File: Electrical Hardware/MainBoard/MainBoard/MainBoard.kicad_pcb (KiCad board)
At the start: 2 copper layers, 49.4 x 51.7 mm, 76 parts, among them J1 SM02B-SRSS-TB_LFSN_, J2 Conn_01x04_Socket, J3 Conn_01x04_Socket, J4 Conn_01x04_Socket, J5 USB_B_Micro, J6 Thermistor, J7 62684-401100ALF, J8 Conn_01x02_Socket, SW1 SW_Push, SW2 SW_Push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

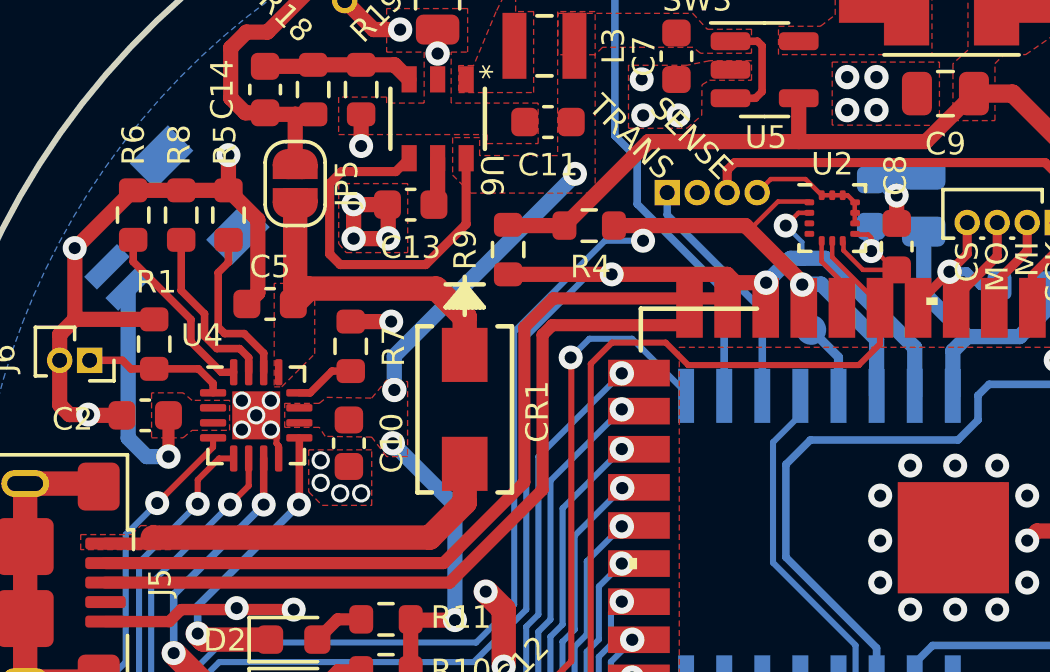
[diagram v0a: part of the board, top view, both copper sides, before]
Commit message: Expand LIS2D and BQ24074 footprint pads
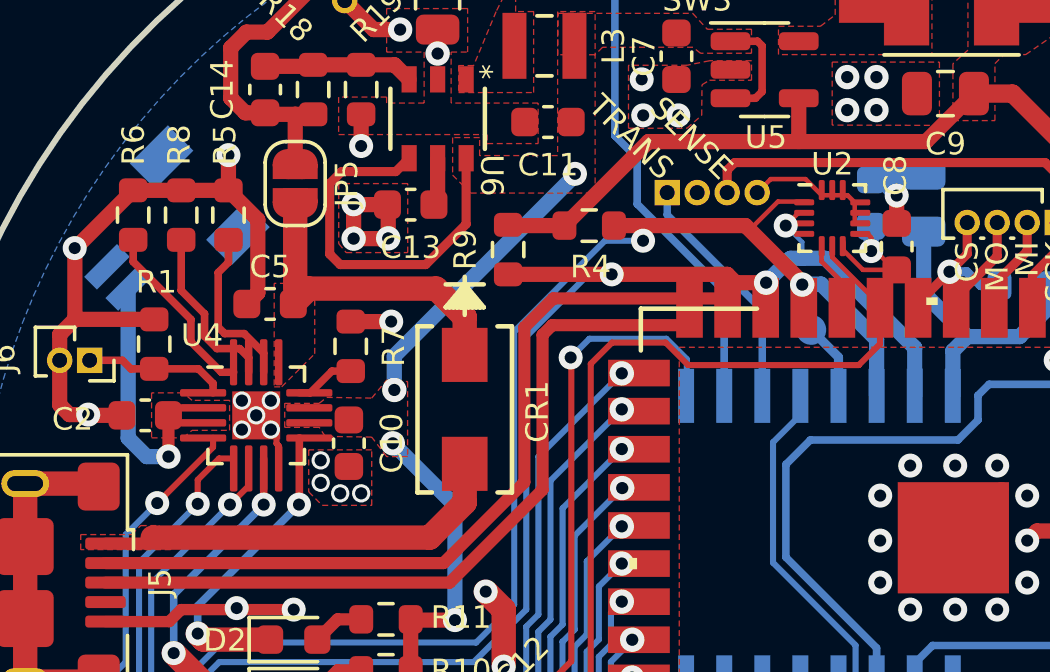
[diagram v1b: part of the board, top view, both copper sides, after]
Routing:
- net /BACKLIGHT: track 22.3 -> 23.0 mm

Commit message: LIS2d Layout
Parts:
- moved C8 1.71 mm to (101.2, 38.2)
- moved U2 0.84 mm to (99.1, 38.8)
- moved R3 0.27 mm to (108.7, 39.0)
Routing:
- net /CS: track 5.95 -> 2.59 mm, vias 1 -> 0
- net GND: track 150.5 -> 152.4 mm
- net /SENSE_P: track 17.8 -> 18.6 mm
- net Net-(JP1-B): track 13.2 -> 13.7 mm
- net +3.3V: track 138.5 -> 138.2 mm, vias 7 -> 6

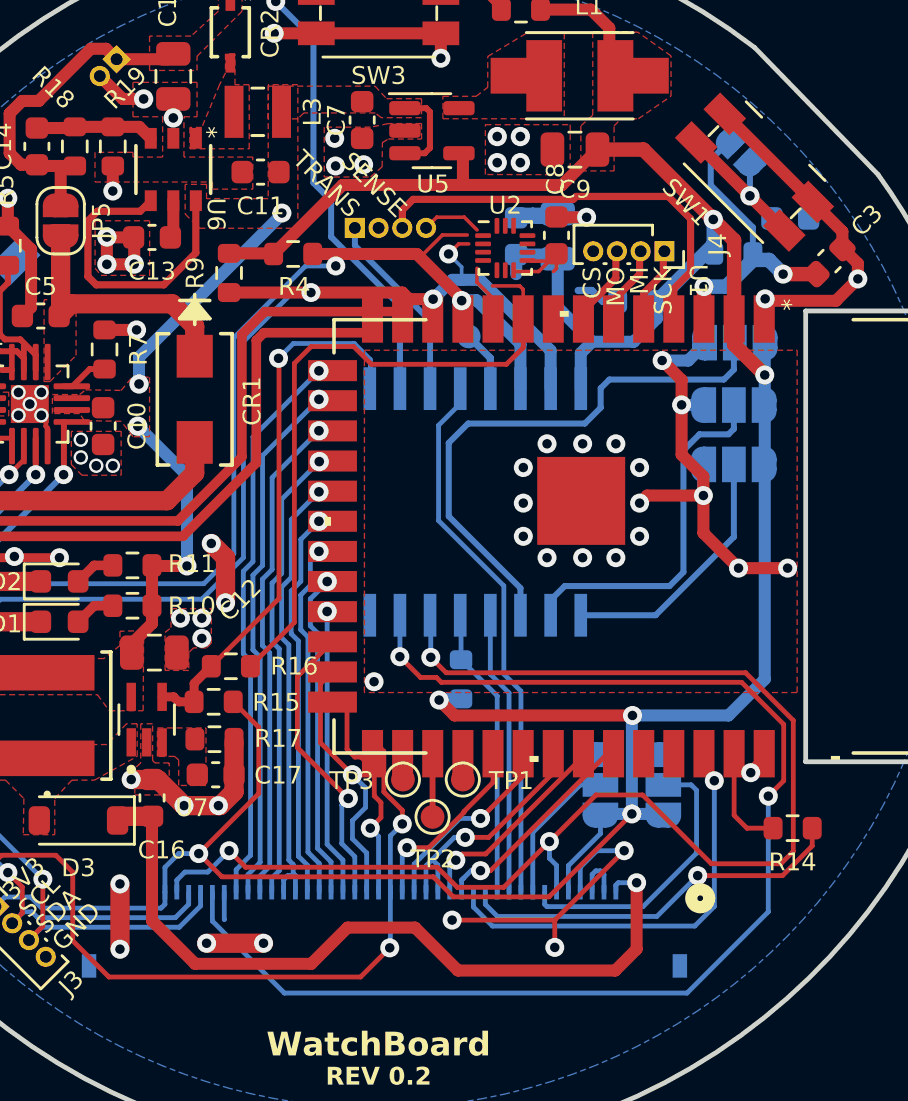
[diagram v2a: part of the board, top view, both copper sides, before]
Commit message: Wire LEDK and adjust wiring
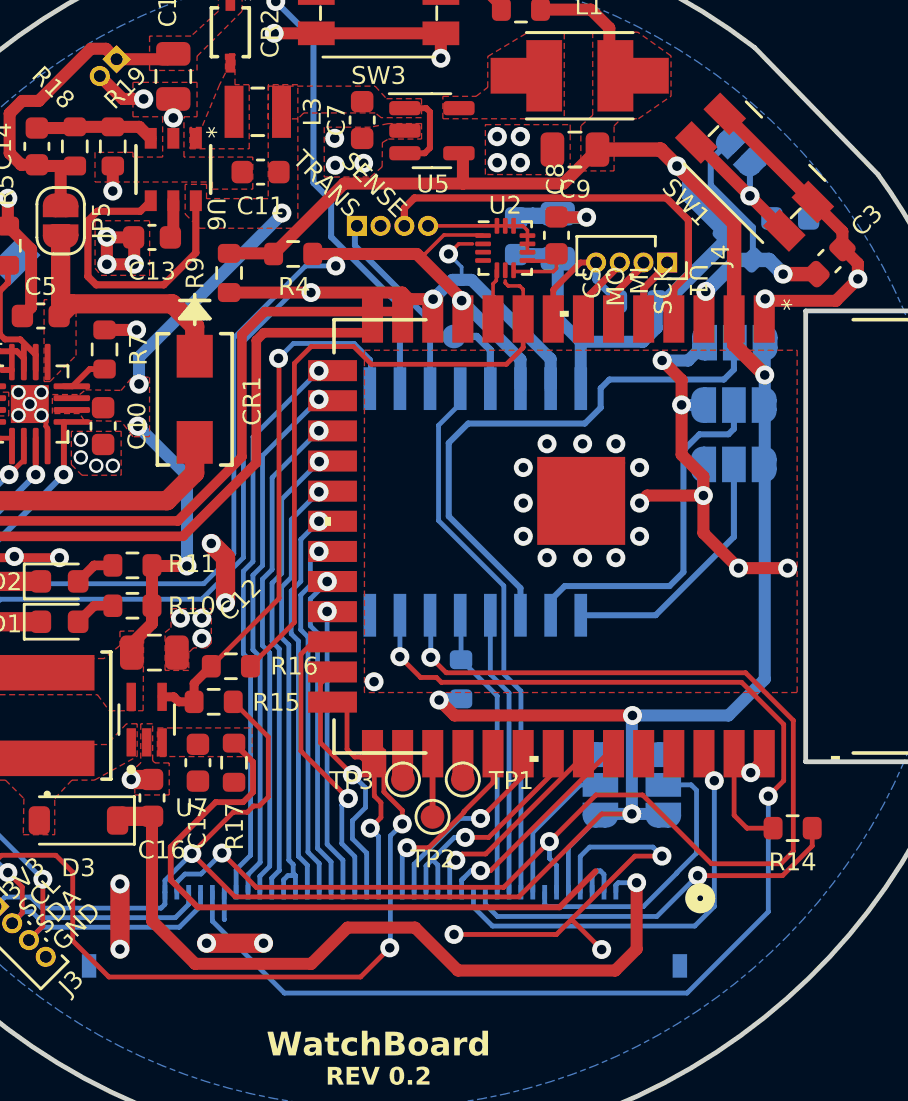
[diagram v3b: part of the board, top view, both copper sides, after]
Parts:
- moved R17 1.29 mm to (87.6, 60.5), turned to -90 degrees
- moved C17 0.91 mm to (86.1, 60.5), turned to -90 degrees
- moved TP4 0.62 mm to (96.9, 42.5)
- moved J4 0.49 mm to (105.9, 39.4)
- moved R3 0.39 mm to (108.9, 38.7), turned to -45 degrees
- moved J2 0.12 mm to (92.8, 37.8)
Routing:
- net /LEDK: track 2.12 -> 29.3 mm
- net +3.3V: track 138.2 -> 144.4 mm
- net /CS: track 2.59 -> 6.26 mm
- net /EXP_IRQ: track 2.58 -> 3.40 mm
- net GND: track 152.4 -> 153.2 mm, vias 68 -> 66

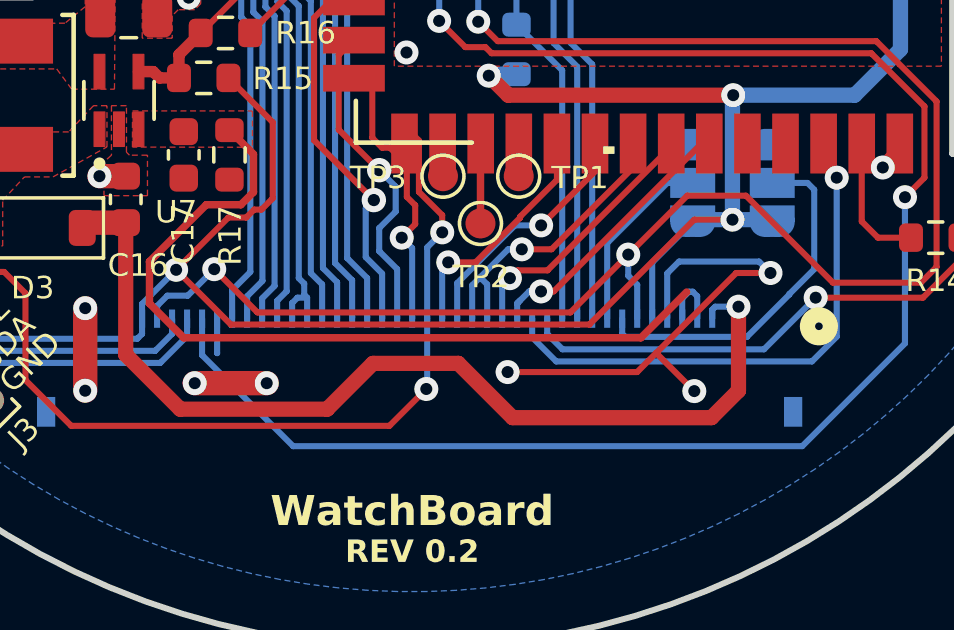
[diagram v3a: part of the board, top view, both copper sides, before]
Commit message: Finish first pass LEDK wiring fix
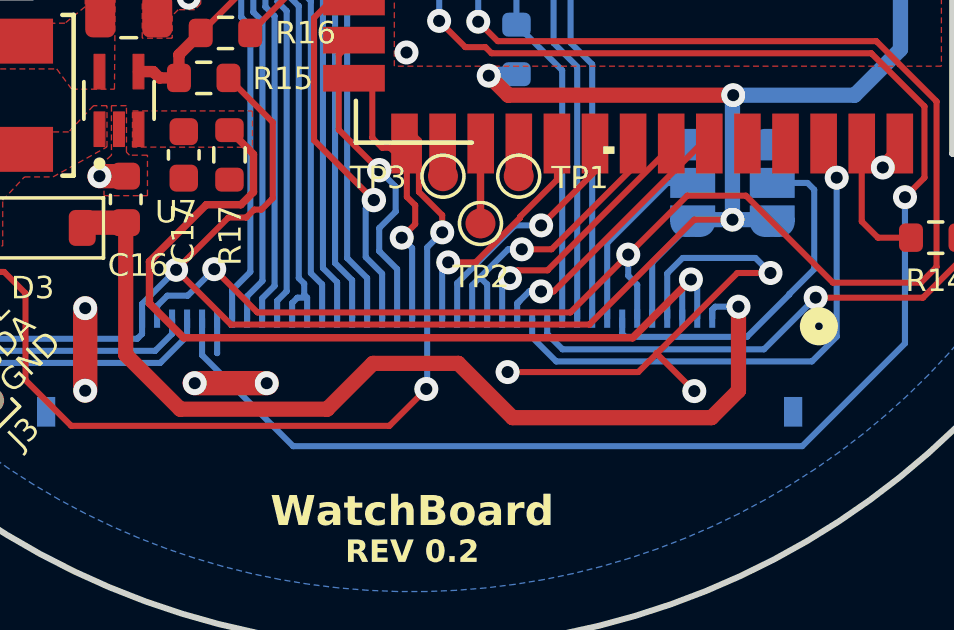
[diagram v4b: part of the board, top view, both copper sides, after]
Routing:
- net /LEDK: track 29.3 -> 30.4 mm, vias 0 -> 1
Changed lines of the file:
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@@
   (segment (start 78.0967 37.8367) (end 74.9217 37.8367) (width 0.508) (layer "F.Cu") (net 1))
   (segment (start 82.519198 36.359174) (end 82.519186 36.359186) (width 0.508) (layer "F.Cu") (net 1))
+  (segment (start 101.257421 67.691002) (end 104.559431 64.388992) (width 0.2032) (layer "F.Cu") (net 1))
   (segment (start 72.6217 57.9117) (end 71.4217 57.9117) (width 0.508) (layer "F.Cu") (net 1))
   (segment (start 99.8027 37.8267) (end 99.995 38.019) (width 0.1524) (layer "F.Cu") (net 1))
@@
   (segment (start 82.269202 39.44595) (end 83.412454 39.44595) (width 0.508) (layer "F.Cu") (net 1))
   (segment (start 96.3467 29.7117) (end 96.3467 30.7617) (width 0.508) (layer "F.Cu") (net 1))
-  (segment (start 101.1467 67.691002) (end 96.901 67.691002) (width 0.2032) (layer "F.Cu") (net 1))
   (segment (start 109.9754 60.304402) (end 109.407 60.872802) (width 0.508) (layer "F.Cu") (net 1))
   (segment (start 79.6983 46.278215) (end 79.6983 46.0133) (width 0.2032) (layer "F.Cu") (net 1))
@@
   (segment (start 113.9217 40.0617) (end 113.9217 40.0617) (width 0.508) (layer "F.Cu") (net 1))
   (segment (start 71.3217 54.2117) (end 73.6717 54.2117) (width 0.8128) (layer "F.Cu") (net 1))
-  (segment (start 101.1467 67.691002) (end 101.218998 67.691002) (width 0.2032) (layer "F.Cu") (net 1))
   (segment (start 79.7717 46.7742) (end 79.7717 46.351615) (width 0.2032) (layer "F.Cu") (net 1))
   (segment (start 72.7967 45.3117) (end 73.4217 45.3117) (width 0.508) (layer "F.Cu") (net 1))
@@
   (segment (start 113.921726 40.0617) (end 112.998041 40.985385) (width 0.508) (layer "F.Cu") (net 1))
   (segment (start 99.41 37.8267) (end 99.8027 37.8267) (width 0.1524) (layer "F.Cu") (net 1))
-  (segment (start 104.521008 64.388992) (end 105.664 64.388992) (width 0.2032) (layer "F.Cu") (net 1))
   (segment (start 72.4717 42.6421) (end 72.4717 43.5017) (width 0.508) (layer "F.Cu") (net 1))
   (segment (start 88.871696 68.0617) (end 88.871698 68.061702) (width 0.508) (layer "F.Cu") (net 1))
@@
   (segment (start 78.3217 51.8117) (end 78.3717 51.7617) (width 0.381) (layer "F.Cu") (net 1))
   (segment (start 82.519198 35.30245) (end 82.519198 36.359174) (width 0.508) (layer "F.Cu") (net 1))
+  (segment (start 96.901 67.691002) (end 101.257421 67.691002) (width 0.2032) (layer "F.Cu") (net 1))
   (segment (start 106.4917 44.321656) (end 105.671738 43.501694) (width 0.508) (layer "F.Cu") (net 1))
   (segment (start 71.3217 47.6117) (end 71.3217 49.7117) (width 0.8128) (layer "F.Cu") (net 1))
-  (segment (start 101.218998 67.691002) (end 104.521008 64.388992) (width 0.2032) (layer "F.Cu") (net 1))
   (segment (start 76.1217 52.2117) (end 76.5217 51.8117) (width 0.381) (layer "F.Cu") (net 1))
   (segment (start 71.3217 47.6117) (end 73.6717 47.6117) (width 0.8128) (layer "F.Cu") (net 1))
@@
   (segment (start 78.4217 51.8117) (end 80.2717 51.8117) (width 0.381) (layer "F.Cu") (net 1))
   (segment (start 79.47955 45.79455) (end 79.5233 45.79455) (width 0.2032) (layer "F.Cu") (net 1))
+  (segment (start 104.559431 64.388992) (end 105.664 64.388992) (width 0.2032) (layer "F.Cu") (net 1))
   (segment (start 106.4917 45.3717) (end 106.4917 47.4717) (width 0.508) (layer "F.Cu") (net 1))
   (segment (start 106.4917 45.3717) (end 106.4917 44.321656) (width 0.508) (layer "F.Cu") (net 1))
@@
   (segment (start 87.217542 65.9117) (end 87.217542 67.057542) (width 0.2032) (layer "B.Cu") (net 1))
   (segment (start 106.774206 43.501694) (end 105.671738 43.501694) (width 0.508) (layer "B.Cu") (net 1))
+  (segment (start 102.221322 65.9117) (end 102.221322 64.402814) (width 0.2032) (layer "B.Cu") (net 1))
   (segment (start 102.4673 37.4867) (end 102.489 37.465) (width 0.508) (layer "B.Cu") (net 1))
   (segment (start 99.6967 37.3117) (end 99.5217 37.4867) (width 0.508) (layer "B.Cu") (net 1))
   (segment (start 100.2217 37.3117) (end 99.6967 37.3117) (width 0.508) (layer "B.Cu") (net 1))
-  (segment (start 105.283008 64.008) (end 105.664 64.388992) (width 0.2032) (layer "B.Cu") (net 1))
+  (segment (start 102.221322 64.402814) (end 102.736736 63.8874) (width 0.2032) (layer "B.Cu") (net 1))
   (segment (start 73.3967 61.6717) (end 72.2467 60.5217) (width 0.8128) (layer "B.Cu") (net 1))
   (segment (start 101.2717 37.3117) (end 100.2217 37.3117) (width 0.508) (layer "B.Cu") (net 1))
-  (segment (start 102.221322 65.9117) (end 102.221322 64.402678) (width 0.2032) (layer "B.Cu") (net 1))
-  (segment (start 102.221322 64.402678) (end 102.616 64.008) (width 0.2032) (layer "B.Cu") (net 1))
+  (segment (start 105.162408 63.8874) (end 105.664 64.388992) (width 0.2032) (layer "B.Cu") (net 1))
   (segment (start 72.2467 59.1717) (end 71.4217 58.3467) (width 0.8128) (layer "B.Cu") (net 1))
   (segment (start 107.3967 45.3792) (end 106.4992 45.3792) (width 0.508) (layer "B.Cu") (net 1))
@@
   (segment (start 72.2467 60.5217) (end 72.2467 59.1717) (width 0.8128) (layer "B.Cu") (net 1))
   (segment (start 100.375 37.465) (end 102.489 37.465) (width 0.508) (layer "B.Cu") (net 1))
+  (segment (start 102.736736 63.8874) (end 105.162408 63.8874) (width 0.2032) (layer "B.Cu") (net 1))
   (segment (start 99.5217 37.4867) (end 102.4673 37.4867) (width 0.508) (layer "B.Cu") (net 1))
   (segment (start 107.3967 42.8792) (end 106.774206 43.501694) (width 0.508) (layer "B.Cu") (net 1))
@@
   (segment (start 107.3967 49.176702) (end 107.411698 49.1917) (width 0.508) (layer "B.Cu") (net 1))
   (segment (start 100.2217 37.3117) (end 100.375 37.465) (width 0.508) (layer "B.Cu") (net 1))
-  (segment (start 102.616 64.008) (end 105.283008 64.008) (width 0.2032) (layer "B.Cu") (net 1))
   (segment (start 107.110951 34.310138) (end 106.957471 34.156658) (width 0.508) (layer "F.Cu") (net 2))
   (segment (start 110.823262 38.022449) (end 107.110951 34.310138) (width 0.508) (layer "F.Cu") (net 2))
@@
   (segment (start 103.7217 65.6117) (end 103.8217 65.5117) (width 0.2032) (layer "B.Cu") (net 11))
   (segment (start 103.7217 65.9117) (end 103.7217 65.6117) (width 0.2032) (layer "B.Cu") (net 11))
-  (segment (start 86.857538 62.113462) (end 84.963 64.008) (width 0.25) (layer "F.Cu") (net 12))
-  (segment (start 101.346 66.548) (end 102.87 65.024) (width 0.25) (layer "F.Cu") (net 12))
-  (segment (start 88.43 60.427) (end 88.43 61.694462) (width 0.25) (layer "F.Cu") (net 12))
-  (segment (start 87.63 59.627) (end 88.43 60.427) (width 0.25) (layer "F.Cu") (net 12))
-  (segment (start 86.106 66.548) (end 101.346 66.548) (width 0.25) (layer "F.Cu") (net 12))
-  (segment (start 88.011 62.113462) (end 86.857538 62.113462) (width 0.25) (layer "F.Cu") (net 12))
   (segment (start 84.963 65.405) (end 86.106 66.548) (width 0.25) (layer "F.Cu") (net 12))
   (segment (start 88.43 61.694462) (end 88.011 62.113462) (width 0.25) (layer "F.Cu") (net 12))
+  (segment (start 88.011 62.113462) (end 86.857538 62.113462) (width 0.25) (layer "F.Cu") (net 12))
+  (segment (start 86.857538 62.113462) (end 84.963 64.008) (width 0.25) (layer "F.Cu") (net 12))
+  (segment (start 101.068353 66.548) (end 103.011646 64.604707) (width 0.25) (layer "F.Cu") (net 12))
+  (segment (start 86.106 66.548) (end 101.068353 66.548) (width 0.25) (layer "F.Cu") (net 12))
+  (segment (start 87.63 59.627) (end 88.43 60.427) (width 0.25) (layer "F.Cu") (net 12))
   (segment (start 84.963 64.008) (end 84.963 65.405) (width 0.25) (layer "F.Cu") (net 12))
-  (segment (start 102.94451 65.0117) (end 103.071448 65.0117) (width 0.2032) (layer "B.Cu") (net 12))
-  (segment (start 102.721448 65.234762) (end 102.94451 65.0117) (width 0.2032) (layer "B.Cu") (net 12))
-  (segment (start 102.721448 65.9117) (end 102.721448 65.234762) (width 0.2032) (layer "B.Cu") (net 12))
-  (segment (start 103.071448 65.0117) (end 103.221574 65.161826) (width 0.2032) (layer "B.Cu") (net 12))
-  (segment (start 103.221574 65.161826) (end 103.221574 65.9117) (width 0.2032) (layer "B.Cu") (net 12))
+  (segment (start 88.43 60.427) (end 88.43 61.694462) (width 0.25) (layer "F.Cu") (net 12))
+  (via (at 103.011646 64.604707) (size 0.8) (drill 0.4) (layers "F.Cu" "B.Cu") (net 12))
+  (segment (start 102.721448 65.9117) (end 102.721448 64.894905) (width 0.2032) (layer "B.Cu") (net 12))
+  (segment (start 103.221574 64.814635) (end 103.011646 64.604707) (width 0.2032) (layer "B.Cu") (net 12))
+  (segment (start 102.721448 64.894905) (end 103.011646 64.604707) (width 0.2032) (layer "B.Cu") (net 12))
+  (segment (start 103.221574 65.9117) (end 103.221574 64.814635) (width 0.2032) (layer "B.Cu") (net 12))
   (segment (start 79.4842 54.5117) (end 77.521704 54.5117) (width 0.8128) (layer "F.Cu") (net 13))
   (segment (start 77.521704 54.5117) (end 76.271704 53.2617) (width 0.8128) (layer "F.Cu") (net 13))
